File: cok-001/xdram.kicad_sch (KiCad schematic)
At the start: 38 parts, among them U1201 Y0_XDR0, U1202 Y0_XDR1, U1301 Y1_XDR0, U1302 Y1_XDR1

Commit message: seperate out
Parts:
- added C1343, C1344, C1345, C1346, C1347, C1348, C1349, C1350, C1351, C1352, C1353, C1354, C1355, C1356, C1357, C1358, C1359, C1360, C1361, C1362, C1363, C1364, C1365, C1366, C1367, C1368, C1369, C1370: 0.1u 10V, Capacitor_SMD:C_0402_1005Metric, symbol Device:C
- added C1609, C1610: 1u 10V, Capacitor_SMD:C_0402_1005Metric, symbol Device:C
- added C1611, C1612: 10u 6.3V, Capacitor_SMD:C_0402_1005Metric, symbol Device:C
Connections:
- net +1.2V_YC_RC_VDDIO: now also C1345.1, C1348.1, C1351.1, C1354.1, C1357.1, C1360.1, C1363.1, C1366.1, C1369.1, C1370.1, C1610.1, C1612.1
- net +1.8V_VDD_MEM: now also C1343.1, C1344.1, C1346.1, C1347.1, C1349.1, C1350.1, C1352.1, C1353.1, C1355.1, C1356.1, C1358.1, C1359.1, C1361.1, C1362.1, C1364.1, C1365.1, C1367.1, C1368.1, C1609.1, C1611.1
- net GND: now also C1343.2, C1344.2, C1345.2, C1346.2, C1347.2, C1348.2, C1349.2, C1350.2, C1351.2, C1352.2, C1353.2, C1354.2, C1355.2, C1356.2, C1357.2, C1358.2, C1359.2, C1360.2, C1361.2, C1362.2, C1363.2, C1364.2, C1365.2, C1366.2, C1367.2, C1368.2, C1369.2, C1370.2, C1609.2, C1610.2, C1611.2, C1612.2
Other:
- moved on the sheet: C1313, C1314, C1316, C1317, C1318, C1319, C1320, C1322, C1323, C1324, C1325, C1326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

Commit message: update to 9
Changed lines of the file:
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@@
 (kicad_sch
-	(version 20231120)
+	(version 20250114)
 	(generator "eeschema")
-	(generator_version "8.0")
+	(generator_version "9.0")
 	(paper "A3")
+	(text_box "Y1 XDR0 DECAP"
+		(exclude_from_sim no)
+		(at 309.88 185.42 0)
+		(size 111.76 85.09)
+		(margins 0.9525 0.9525 0.9525 0.9525)
+		(stroke
+			(width 0)
+			(type default)
+		)
+		(fill
+			(type none)
+		)
+		(effects
+			(font
+				(size 1.27 1.27)
+			)
+			(justify left top)
+		)
+	)
+	(text_box "Y1 XDR0 DECAP"
+		(exclude_from_sim no)
+		(at 193.04 185.42 0)
+		(size 111.76 85.09)
+		(margins 0.9525 0.9525 0.9525 0.9525)
+		(stroke
+			(width 0)
+			(type default)
+		)
+		(fill
+			(type none)
+		)
+		(effects
+			(font
+				(size 1.27 1.27)
+			)
+			(justify left top)
+		)
+	)
 	(junction
 		(at 72.39 147.32)
@@
 		)
 	)
-	(text_box "Y1 XDR0 DECAP"
-		(exclude_from_sim no)
-		(at 309.88 185.42 0)
-		(size 111.76 85.09)
-		(stroke
-			(width 0)
-			(type default)
-		)
-		(fill
-			(type none)
-		)
-		(effects
-			(font
-				(size 1.27 1.27)
-			)
-			(justify left top)
-		)
-	)
-	(text_box "Y1 XDR0 DECAP"
-		(exclude_from_sim no)
-		(at 193.04 185.42 0)
-		(size 111.76 85.09)
-		(stroke
-			(width 0)
-			(type default)
-		)
-		(fill
-			(type none)
-		)
-		(effects
-			(font
-				(size 1.27 1.27)
-			)
-			(justify left top)
-		)
-	)

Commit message: cell
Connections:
- net Y0_XDR1_RQ0 is gone; now on net BE_Y0_RQ0: U1202.C3 (RQ0)
- net Y0_XDR1_RQ1 is gone; now on net BE_Y0_RQ1: U1202.D13 (RQ1)
- net Y0_XDR1_RQ10 is gone; now on net BE_Y0_RQ10: U1202.H3 (RQ10)
- net Y0_XDR1_RQ11 is gone; now on net BE_Y0_RQ11: U1202.H4 (RQ11)
- net Y0_XDR1_RQ2 is gone; now on net BE_Y0_RQ2: U1202.D14 (RQ2)
- net Y0_XDR1_RQ3 is gone; now on net BE_Y0_RQ3: U1202.D4 (RQ3)
- net Y0_XDR1_RQ4 is gone; now on net BE_Y0_RQ4: U1202.D3 (RQ4)
- net Y0_XDR1_RQ5 is gone; now on net BE_Y0_RQ5: U1202.E14 (RQ5)
- net Y0_XDR1_RQ6 is gone; now on net BE_Y0_RQ6: U1202.G14 (RQ6)
- net Y0_XDR1_RQ7 is gone; now on net BE_Y0_RQ7: U1202.G13 (RQ7)
- net Y0_XDR1_RQ8 is gone; now on net BE_Y0_RQ8: U1202.H14 (RQ8)
- net Y0_XDR1_RQ9 is gone; now on net BE_Y0_RQ9: U1202.H13 (RQ9)
- net Y1_XDR1_RQ0 is gone; now on net BE_Y1_RQ0: U1302.C3 (RQ0)
- net Y1_XDR1_RQ1 is gone; now on net BE_Y1_RQ1: U1302.D13 (RQ1)
- net Y1_XDR1_RQ10 is gone; now on net BE_Y1_RQ10: U1302.H3 (RQ10)
- net Y1_XDR1_RQ11 is gone; now on net BE_Y1_RQ11: U1302.H4 (RQ11)
- net Y1_XDR1_RQ2 is gone; now on net BE_Y1_RQ2: U1302.D14 (RQ2)
- net Y1_XDR1_RQ3 is gone; now on net BE_Y1_RQ3: U1302.D4 (RQ3)
- net Y1_XDR1_RQ4 is gone; now on net BE_Y1_RQ4: U1302.D3 (RQ4)
- net Y1_XDR1_RQ5 is gone; now on net BE_Y1_RQ5: U1302.E14 (RQ5)
- net Y1_XDR1_RQ6 is gone; now on net BE_Y1_RQ6: U1302.G14 (RQ6)
- net Y1_XDR1_RQ7 is gone; now on net BE_Y1_RQ7: U1302.G13 (RQ7)
- net Y1_XDR1_RQ8 is gone; now on net BE_Y1_RQ8: U1302.H14 (RQ8)
- net Y1_XDR1_RQ9 is gone; now on net BE_Y1_RQ9: U1302.H13 (RQ9)
- net Y0_XDR0_RQ0 renamed BE_Y0_RQ0
- net Y0_XDR0_RQ1 renamed BE_Y0_RQ1
- net Y0_XDR0_RQ10 renamed BE_Y0_RQ10
- net Y0_XDR0_RQ11 renamed BE_Y0_RQ11
- net Y0_XDR0_RQ2 renamed BE_Y0_RQ2
- net Y0_XDR0_RQ3 renamed BE_Y0_RQ3
- net Y0_XDR0_RQ4 renamed BE_Y0_RQ4
- net Y0_XDR0_RQ5 renamed BE_Y0_RQ5
- net Y0_XDR0_RQ6 renamed BE_Y0_RQ6
- net Y0_XDR0_RQ7 renamed BE_Y0_RQ7
- net Y0_XDR0_RQ8 renamed BE_Y0_RQ8
- net Y0_XDR0_RQ9 renamed BE_Y0_RQ9
- net Y1_XDR0_RQ0 renamed BE_Y1_RQ0
- net Y1_XDR0_RQ1 renamed BE_Y1_RQ1
- net Y1_XDR0_RQ10 renamed BE_Y1_RQ10
- net Y1_XDR0_RQ11 renamed BE_Y1_RQ11
- net Y1_XDR0_RQ2 renamed BE_Y1_RQ2
- net Y1_XDR0_RQ3 renamed BE_Y1_RQ3
- net Y1_XDR0_RQ4 renamed BE_Y1_RQ4
- net Y1_XDR0_RQ5 renamed BE_Y1_RQ5
- net Y1_XDR0_RQ6 renamed BE_Y1_RQ6
- net Y1_XDR0_RQ7 renamed BE_Y1_RQ7
- net Y1_XDR0_RQ8 renamed BE_Y1_RQ8
- net Y1_XDR0_RQ9 renamed BE_Y1_RQ9

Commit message: ram
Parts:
- added Q1201, Q1301: RK7002, Package_TO_SOT_SMD:SOT-23, symbol Transistor_FET_Other:Q_NMOS_Depletion_SGD
- added Q1202, Q1302: SST2222AT, Package_TO_SOT_SMD:SOT-23, symbol Transistor_BJT:MMBT2222A
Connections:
- net GND: now also Q1202.2 (E), Q1302.2 (E)

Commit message: ram lines
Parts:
- added R1225, R1226, R1227, R1228, R1229, R1230, R1231, R1232, R1233, R1234, R1235, R1236, R1325, R1326, R1327, R1328, R1329, R1330, R1331, R1332, R1333, R1334, R1335, R1336: 43.2, Resistor_SMD:R_0402_1005Metric, symbol Device:R_US
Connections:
- net BE_Y0_RQ0: now also R1225.1
- net BE_Y0_RQ1: now also R1226.1
- net BE_Y0_RQ10: now also R1235.1
- net BE_Y0_RQ11: now also R1236.1
- net BE_Y0_RQ2: now also R1227.1
- net BE_Y0_RQ3: now also R1228.1
- net BE_Y0_RQ4: now also R1229.1
- net BE_Y0_RQ5: now also R1230.1
- net BE_Y0_RQ6: now also R1231.1
- net BE_Y0_RQ7: now also R1232.1
- net BE_Y0_RQ8: now also R1233.1
- net BE_Y0_RQ9: now also R1234.1
- net BE_Y1_RQ0: now also R1325.1
- net BE_Y1_RQ1: now also R1326.1
- net BE_Y1_RQ10: now also R1335.1
- net BE_Y1_RQ11: now also R1336.1
- net BE_Y1_RQ2: now also R1327.1
- net BE_Y1_RQ3: now also R1328.1
- net BE_Y1_RQ4: now also R1329.1
- net BE_Y1_RQ5: now also R1330.1
- net BE_Y1_RQ6: now also R1331.1
- net BE_Y1_RQ7: now also R1332.1
- net BE_Y1_RQ8: now also R1333.1
- net BE_Y1_RQ9: now also R1334.1
- new net: R1325.2, R1326.2, R1327.2, R1328.2, R1329.2, R1330.2, R1331.2, R1332.2, R1333.2, R1334.2, R1335.2, R1336.2
- new net: R1225.2, R1226.2, R1227.2, R1228.2, R1229.2, R1230.2, R1231.2, R1232.2, R1233.2, R1234.2, R1235.2, R1236.2

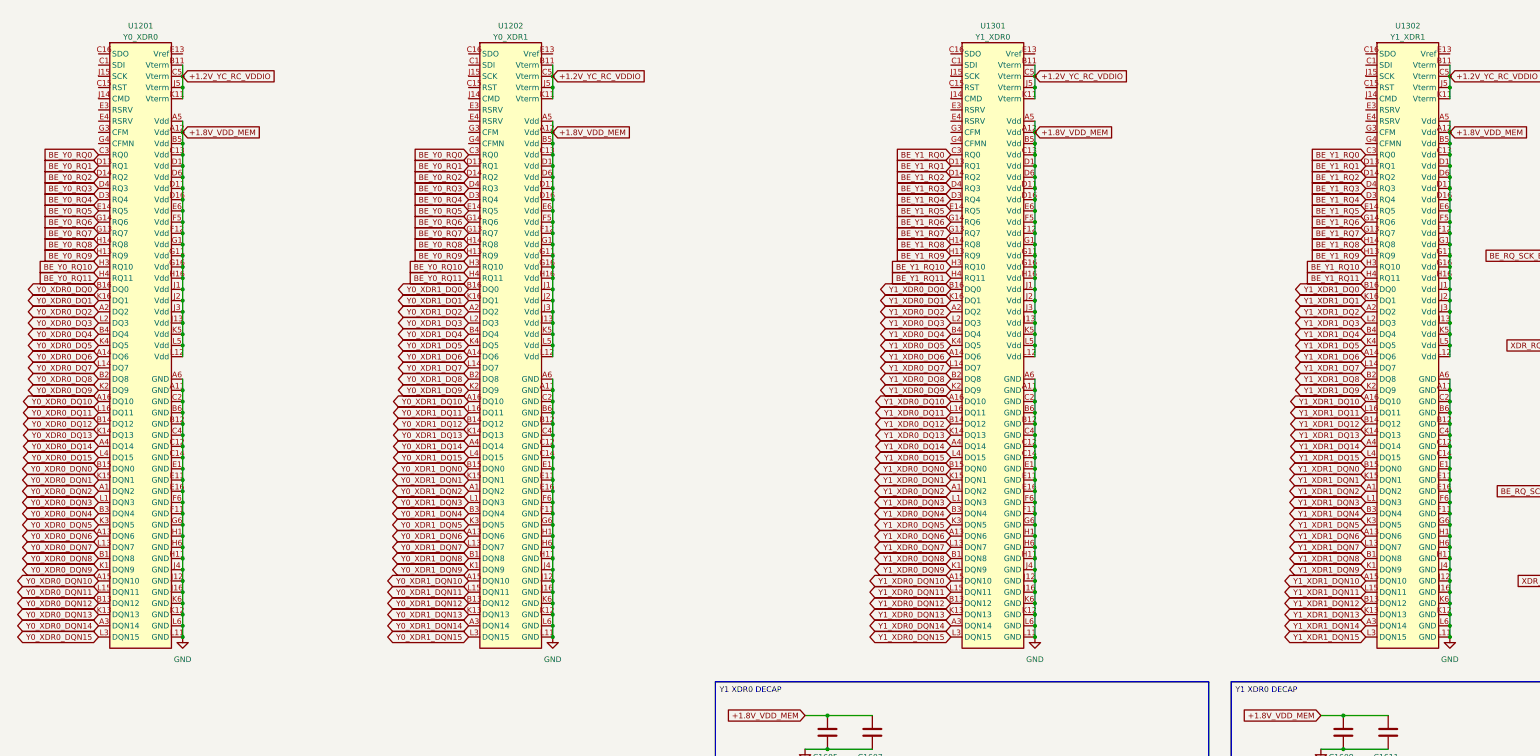
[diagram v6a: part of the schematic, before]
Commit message: ram symbol
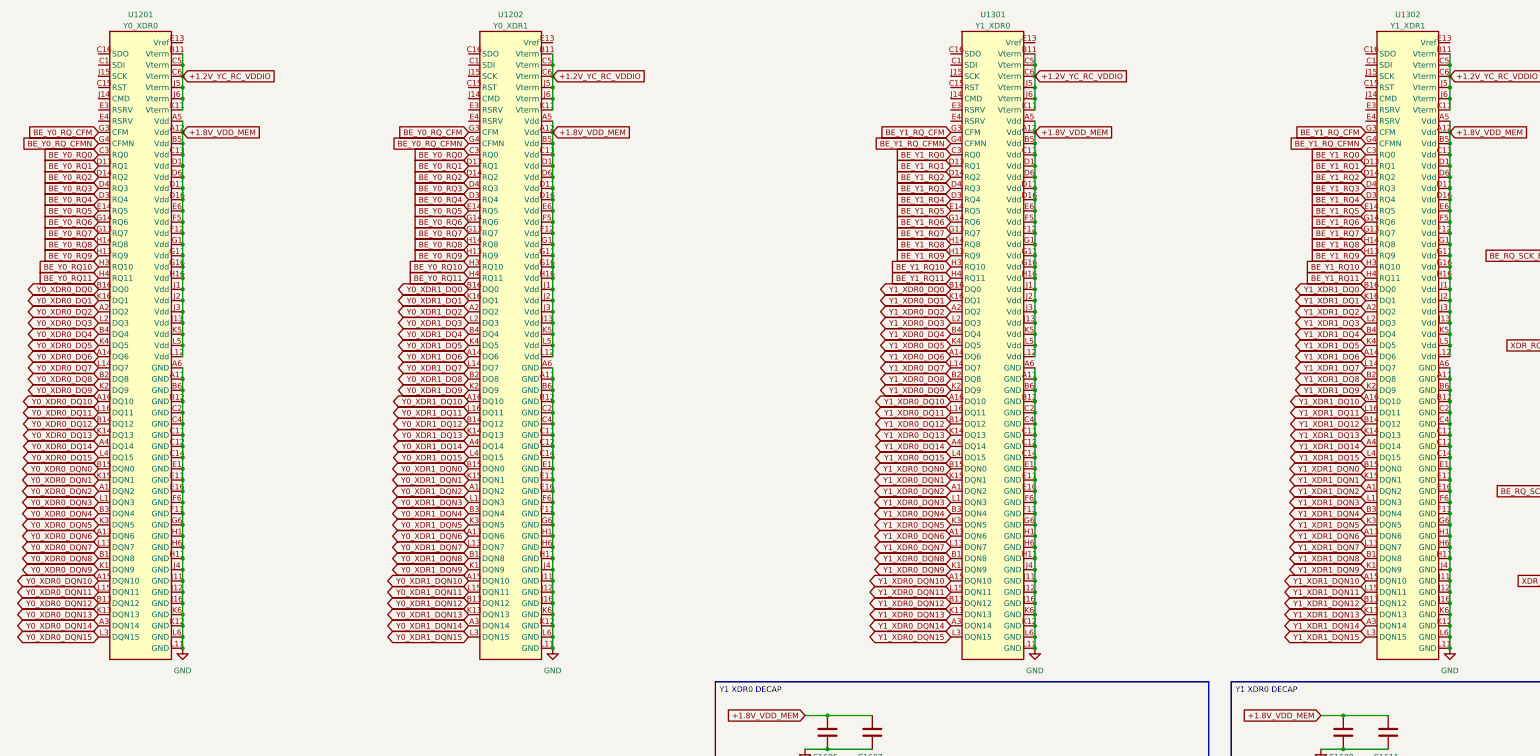
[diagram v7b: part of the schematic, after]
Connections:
- net +1.2V_YC_RC_VDDIO: now also U1201.C6 (Vterm), U1201.J6 (Vterm), U1202.C6 (Vterm), U1202.J6 (Vterm), U1301.C6 (Vterm), U1301.J6 (Vterm), U1302.C6 (Vterm), U1302.J6 (Vterm)
- net GND: now also U1201.C11 (GND), U1201.J11 (GND), U1202.C11 (GND), U1202.J11 (GND), U1301.C11 (GND), U1301.J11 (GND), U1302.C11 (GND), U1302.J11 (GND)
- net BE_Y0_RQ_CFM: now reaches U1201.G3 (CFM)
- net BE_Y0_RQ_CFM: now also U1202.G3 (CFM)
- net BE_Y0_RQ_CFMN: now reaches U1201.G4 (CFMN)
- net BE_Y0_RQ_CFMN: now also U1202.G4 (CFMN)
- net BE_Y1_RQ_CFM: now reaches U1302.G3 (CFM)
- net BE_Y1_RQ_CFM: now also U1301.G3 (CFM)
- net BE_Y1_RQ_CFMN: now reaches U1302.G4 (CFMN)
- net BE_Y1_RQ_CFMN: now also U1301.G4 (CFMN)

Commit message: voltage symbols
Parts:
- added R1204, R1304: 10, Resistor_SMD:R_0805_2012Metric, symbol Device:R_US
- added R1205, R1305: 22.1, Resistor_SMD:R_0805_2012Metric, symbol Device:R_US
- added TP1202, TP1302: TestPoint, TestPoint:TestPoint_Pad_1.0x1.0mm, symbol Connector:TestPoint
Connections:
- net BE_RQ_SCK_BJT: now also Q1202.1 (B), Q1302.1 (B)
- net XDR_RQ_VREF_FET: now also Q1201.2 (G), Q1301.2 (G)
- net BE_Y1_RQ_SCK: now reaches Q1302.3 (C)
- net BE_Y0_RQ_SCK: now reaches Q1202.3 (C)
- net Y0_XDR_RQ_VREF: now reaches Q1201.1 (S)
- net Y0_XDR_RQ_VREF: now also TP1202.1
- net at Q1201.3 (D): now also R1204.2, R1205.1
- net Y1_XDR_RQ_VREF: now reaches Q1301.1 (S)
- net Y1_XDR_RQ_VREF: now also TP1302.1
- net at Q1301.3 (D): now also R1304.2, R1305.1
